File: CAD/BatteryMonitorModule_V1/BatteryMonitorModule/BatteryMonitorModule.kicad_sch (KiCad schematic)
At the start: 72 parts, among them J1 J_FAN, J2 QT06ADP83H0000G, J3 J_NFC, J4 J_PANEL, J5 J_UART, J6 Conn_ARM_JTAG_SWD_10, J7 USB-C, K1 G5Q-14-DC12, Q1 AO4407A, Q2 AO4407A, Q3 AO3400A, Q4 MMBT2222A, Q5 2N7002, SW1 BOOT0, SW2 NRST, U1 STM32C071K8T6, U2 AP63203WU-7, U3 INA226AQDGSRQ1

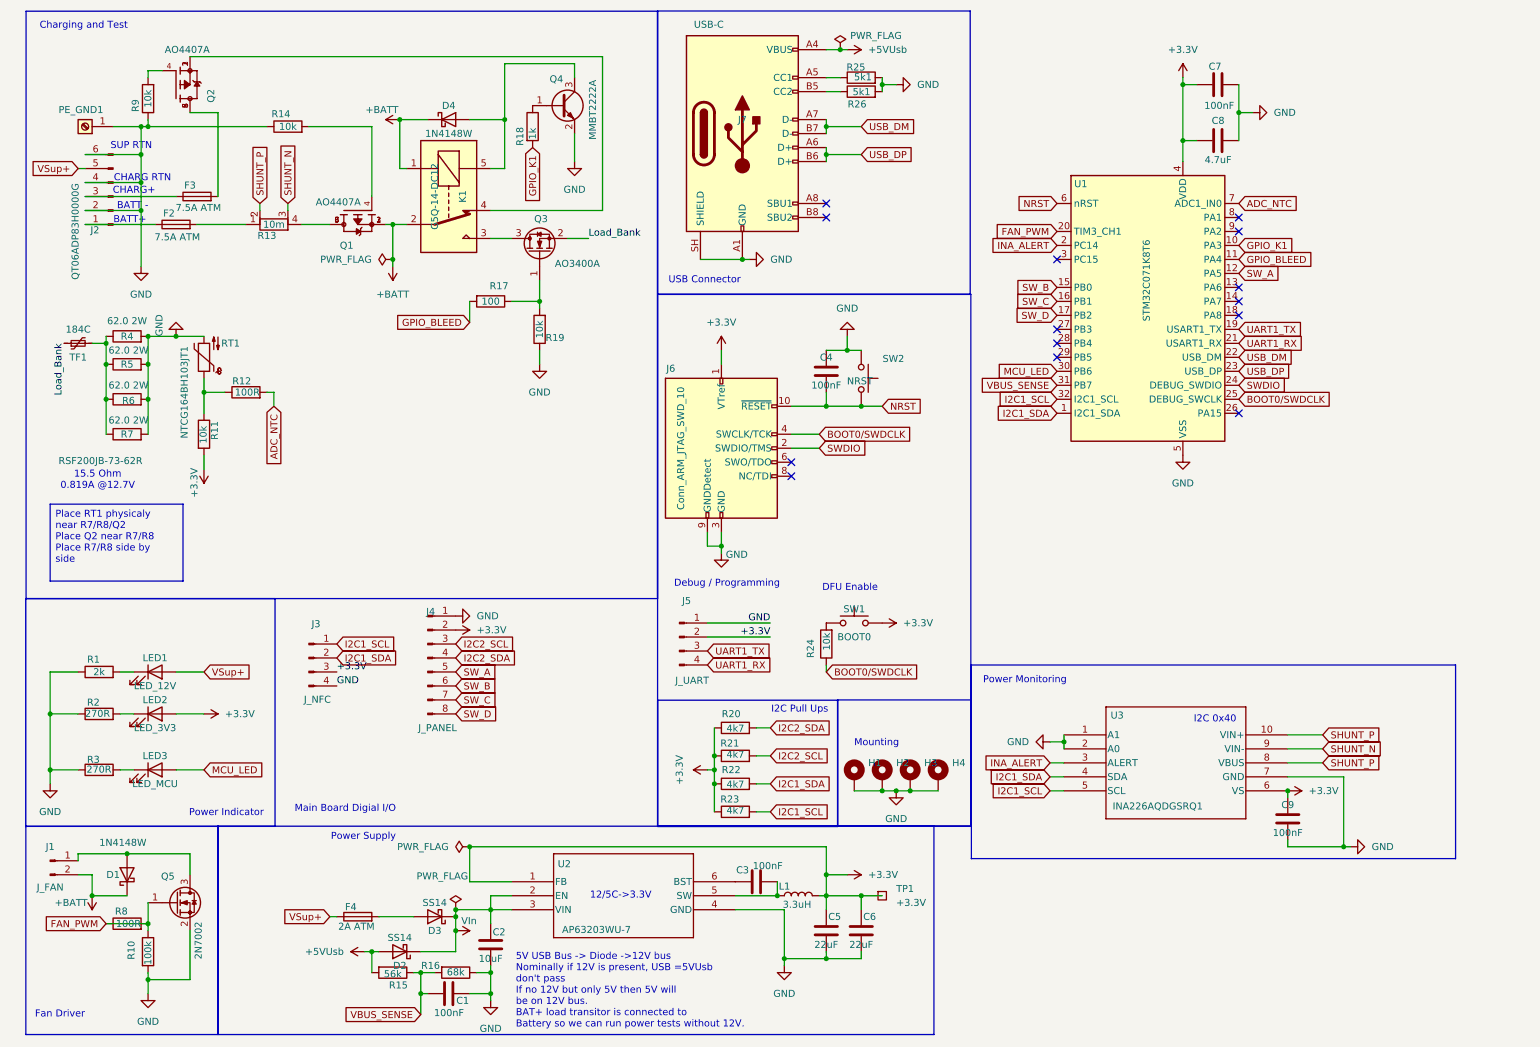
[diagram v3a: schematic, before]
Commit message: V1 PCB layout updates and QT06ADP83H0000G footprint refinement
Co-Authored-By: Claude Opus 4.7 (1M context) <noreply@anthropic.com>
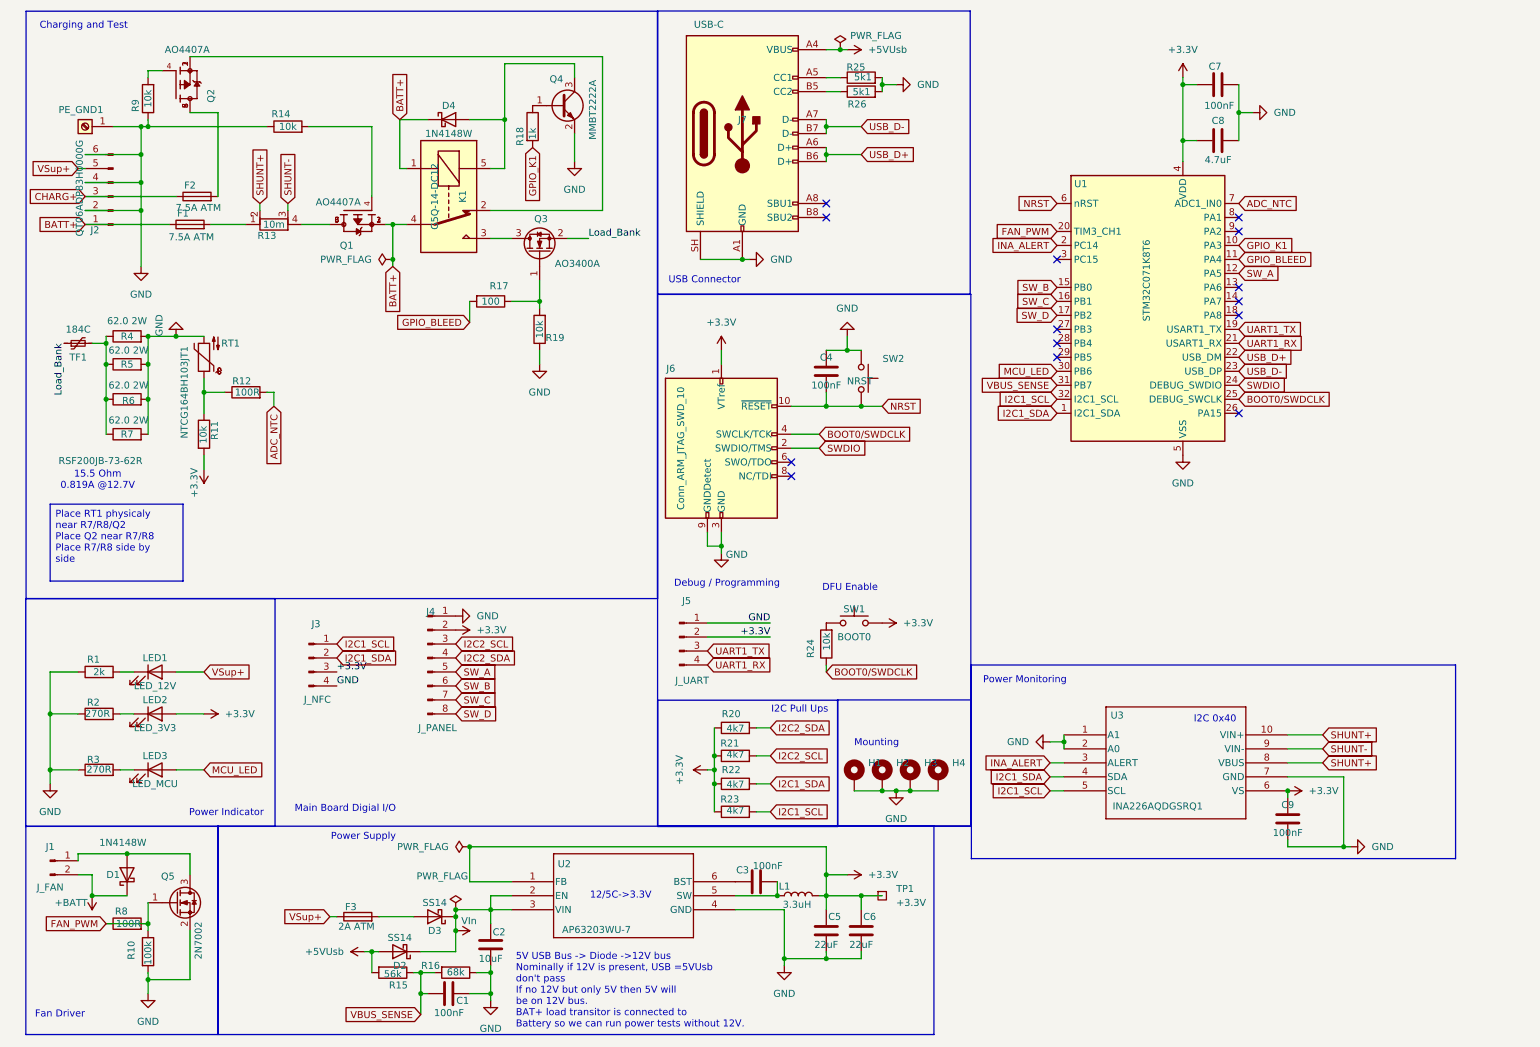
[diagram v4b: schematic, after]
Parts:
- K1: symbol Relay:G5Q-1 -> G5Q-14-fixed:G5Q-1-Fixed
- renumbered F2 to F1, F3 to F2, F4 to F3
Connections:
- net +BATT: no longer D4.1 (K), K1.1, K1.2, Q1.1, Q1.2, Q1.3
- net BATT+: now reaches F1.1, J2.1 (Pin_1)
- net BATT+: now also D4.1 (K), K1.1, K1.4, Q1.1, Q1.2, Q1.3
- net CHARG+: now reaches F2.1, J2.3 (Pin_3)
- net at Q2.1, Q2.2, Q2.3: now also K1.2; no longer K1.4
- net SHUNT_N renamed SHUNT-
- net SHUNT_P renamed SHUNT+
- net USB_DM renamed USB_D-
- net USB_D-: now also U1.23 (PA12); no longer U1.22 (PA11)
- net USB_DP renamed USB_D+
- net USB_D+: now also U1.22 (PA11); no longer U1.23 (PA12)
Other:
- note removed: "BATT -"
- note removed: "BATT+"
- note removed: "CHARG RTN"
- note removed: "CHARG+"
- note removed: "SUP RTN"
- moved on the sheet: F1

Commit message: V1 PCB and schematic updates
Co-Authored-By: Claude Opus 4.7 (1M context) <noreply@anthropic.com>
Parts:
- removed TP1: +3.3V, TestPoint:TestPoint_Pad_2.0x2.0mm, symbol Connector:TestPoint_Square
- added H5: Fan1, BatteryMonitorModule_Custom:2510FanOverhead, symbol Mechanical:MountingHole
- C1: footprint Capacitor_SMD:C_0805_2012Metric -> Capacitor_SMD:C_0402_1005Metric
- C3, C4, C7, C9: footprint Capacitor_SMD:C_0603_1608Metric -> Capacitor_SMD:C_0402_1005Metric
- C8: footprint Capacitor_SMD:C_0805_2012Metric -> Capacitor_SMD:C_0603_1608Metric
- J6: footprint Connector_PinHeader_2.00mm:PinHeader_2x03_P2.00mm_Vertical -> Connector_PinHeader_1.27mm:PinHeader_2x05_P1.27mm_Vertical
- R1: value 2k -> 10k; footprint Resistor_SMD:R_0603_1608Metric -> Resistor_SMD:R_0402_1005Metric
- R10, R11, R14, R15, R16, R17, R18, R19, R24, R25, R26, R9: footprint Resistor_SMD:R_0603_1608Metric -> Resistor_SMD:R_0402_1005Metric
- R12, R8: value 100R -> 100; footprint Resistor_SMD:R_0603_1608Metric -> Resistor_SMD:R_0402_1005Metric
- R2, R3: value 270R -> 5k1; footprint Resistor_SMD:R_0603_1608Metric -> Resistor_SMD:R_0402_1005Metric
- R20, R21, R22, R23: value 4k7 -> 5k1; footprint Resistor_SMD:R_0603_1608Metric -> Resistor_SMD:R_0402_1005Metric
- SW1, SW2: footprint BatteryMonitorModule_Custom:SWITCH_FSMSM_TYC -> Button_Switch_SMD:SW_SPST_FSMSM
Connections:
- net +BATT is gone; now on net BATT+: D1.1 (K), J1.2 (Pin_2)
- net BATT+: no longer F1.1, J2.1 (Pin_1)
- net FAN_PWM: now also U1.10 (PA3); no longer Q5.1 (G), R10.1, R8.2, U1.20 (PC6)
- net GPIO_BLEED: now also U1.9 (PA2); no longer U1.11 (PA4)
- net GPIO_K1: now also U1.8 (PA1); no longer U1.10 (PA3)
- net I2C2_SCL: now also U1.14 (PA7)
- net I2C2_SDA: now also U1.13 (PA6)
- net MCU_LED: now also U1.3 (PC15); no longer U1.30 (PB6)
- net UART1_RX: now also U1.18 (PA8); no longer U1.21 (PA10)
- net +5VUsb renamed +5vuSB
- new net: Q5.1 (G), R10.1, R8.2
- new net BATT_IN+: F1.1, J2.1 (Pin_1)
- no-connect marks 14 -> 12

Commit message: finalize BatteryMonitorModule V1: pcb/sch updates, JST XH 8-pin footprint, gerber export
Co-Authored-By: Claude Opus 4.7 (1M context) <noreply@anthropic.com>
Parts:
- added FID1, FID2, FID3: Fiducial, Fiducial:Fiducial_0.5mm_Mask1.5mm, symbol Mechanical:Fiducial
- added J8: J_PANEL, Connector_PinHeader_2.54mm:PinHeader_2x03_P2.54mm_Vertical, symbol Connector:Conn_01x06_Pin
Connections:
- net +3.3V: now also J8.2 (Pin_2)
- net GND: now also J8.1 (Pin_1)
- net I2C2_SCL: now also J8.3 (Pin_3)
- net I2C2_SDA: now also J8.4 (Pin_4)
- net SW_A: now also J8.5 (Pin_5)
- net SW_B: now also J8.6 (Pin_6)
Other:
- moved on the sheet: H1, H2, H3, H4
